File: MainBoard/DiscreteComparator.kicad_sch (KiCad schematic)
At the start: 22 parts, among them Q17 BC557, Q18 BC557, Q19 BC557, Q20 BC557, Q21 BC557, Q22 BC557, Q23 BC557, Q24 BC557, Q25 BC557, Q26 BC547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

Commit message: dealt j8 pin 2 issue by just leaving pine 2 NC
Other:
- note added: "open-collector"
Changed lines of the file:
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@@
+		)
+	)
+	(text "open-collector"
+		(exclude_from_sim no)
+		(at 217.932 86.868 0)
+		(effects
+			(font
+				(size 1.27 1.27)
+			)
 		)
 	)

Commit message: Added bakers clamp on the inverting output transitors to deal with the transtion voltage spikes
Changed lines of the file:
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@@
 		(dnp no)
 		(property "Reference" "Q28"
-			(at 190.754 94.234 0)
+			(at 193.294 104.648 0)
 			(effects
 				(font
@@
 		)
 		(property "Value" "BC547"
-			(at 190.754 96.774 0)
+			(at 191.008 106.934 0)
 			(effects
 				(font
@@
 		(on_board yes)
 		(dnp no)
-		(fields_autoplaced yes)
 		(property "Reference" "Q29"
-			(at 190.5 104.1399 0)
+			(at 178.816 107.696 0)
 			(effects
 				(font
@@
 		)
 		(property "Value" "BC547"
-			(at 190.5 106.6799 0)
-			(effects
-				(font
+			(at 178.816 110.236 0)
+			(effects
+				(font

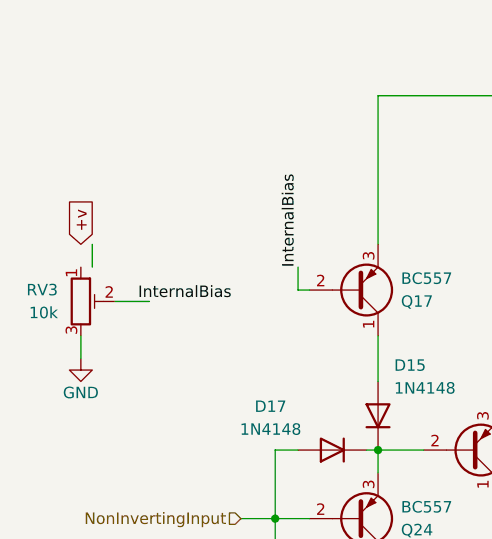
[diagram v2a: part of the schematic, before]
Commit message: added decouping caps to input jack
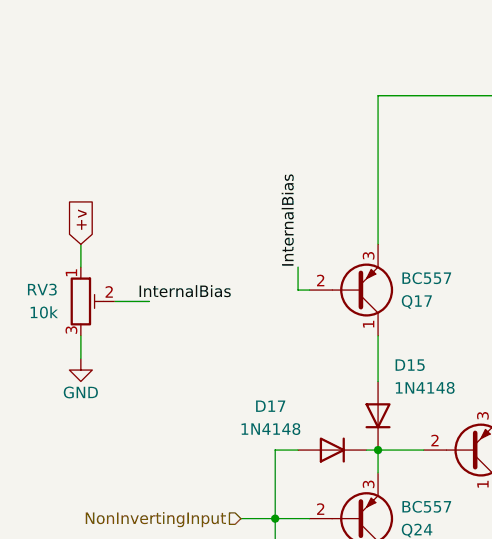
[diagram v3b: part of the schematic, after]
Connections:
- net +v: now also RV3.1
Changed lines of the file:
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@@
 	(wire
 		(pts
-			(xy 68.58 59.69) (xy 68.58 62.23)
+			(xy 67.31 59.69) (xy 67.31 62.23)
 		)
 		(stroke

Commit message: some general clean up
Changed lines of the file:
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@@
 	(wire
 		(pts
-			(xy 71.12 66.04) (xy 74.93 66.04)
+			(xy 71.12 66.04) (xy 73.66 66.04)
 		)
 		(stroke

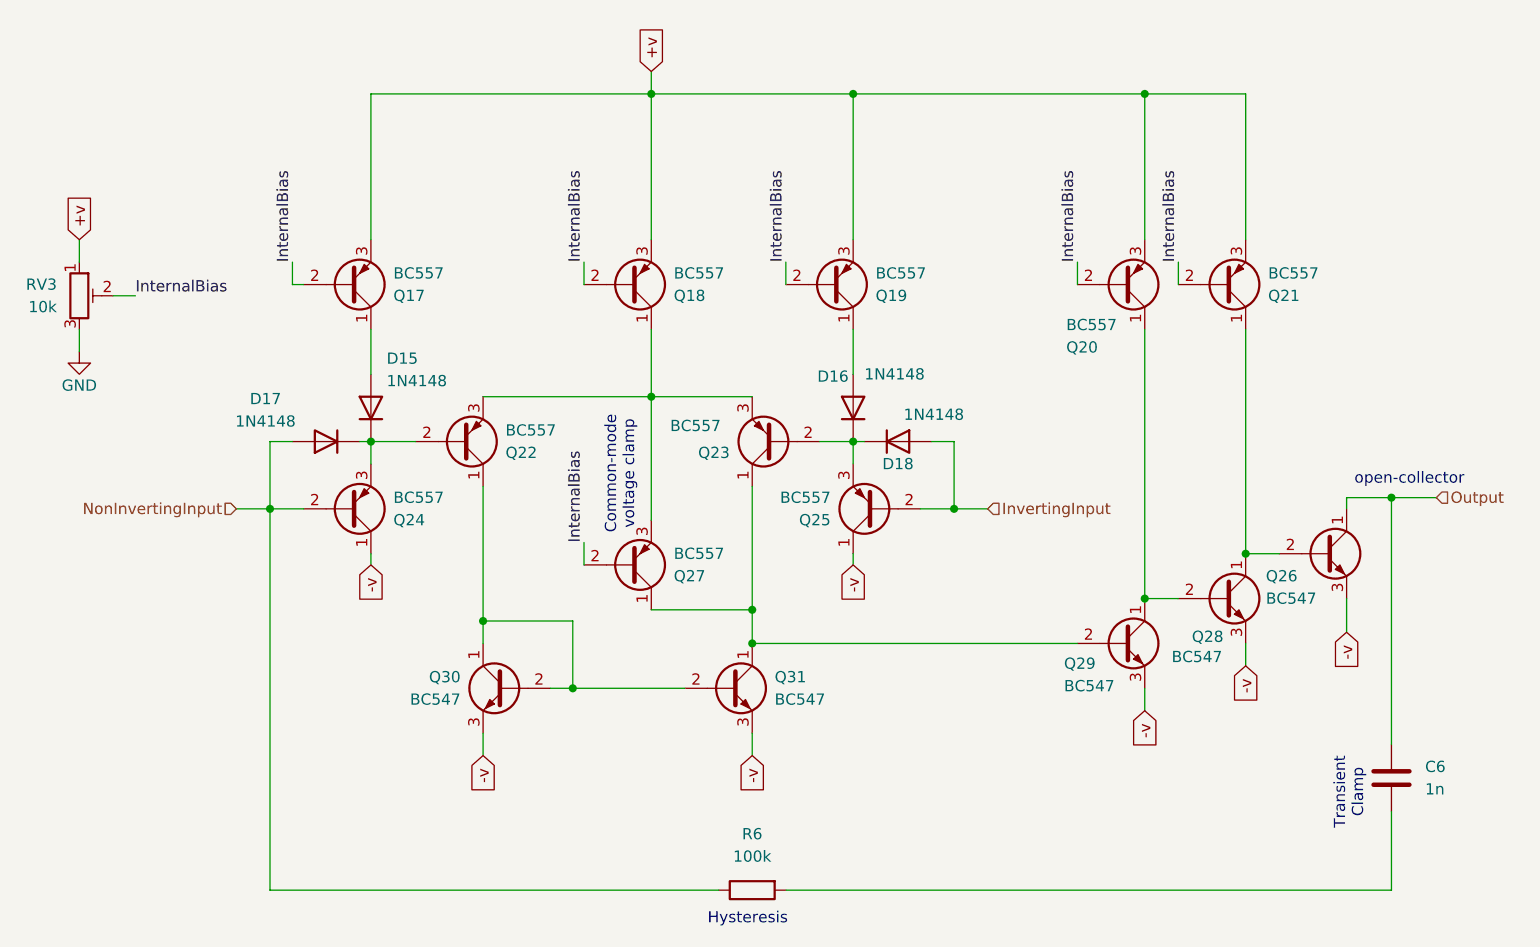
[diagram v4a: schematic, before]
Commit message: refactored power supply
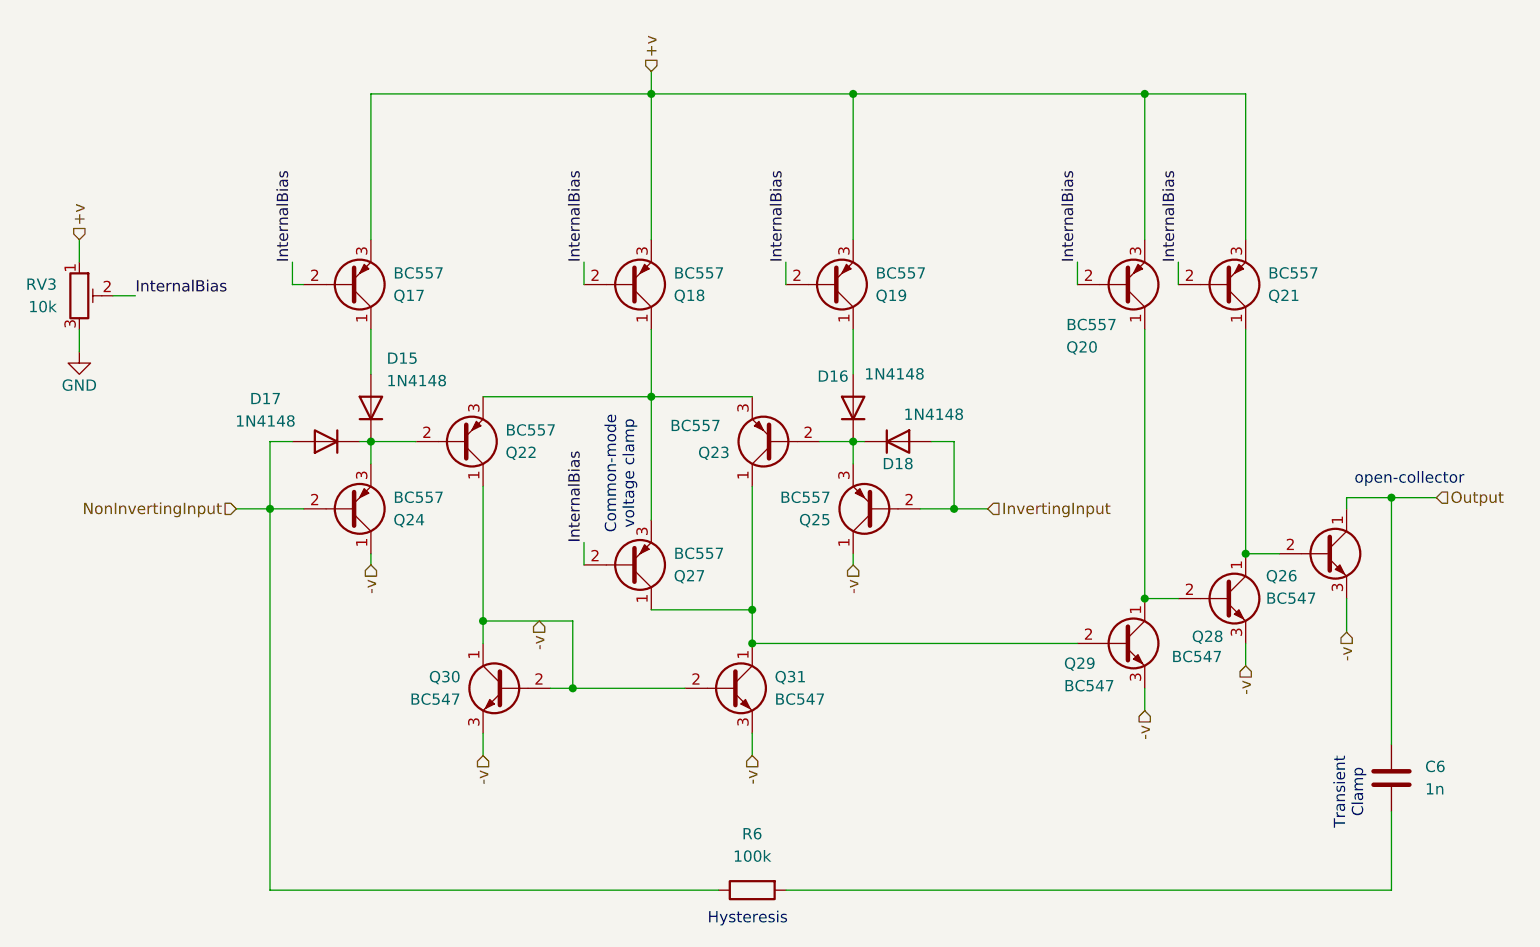
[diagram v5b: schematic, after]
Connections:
- net -v: now also Q22.1 (C), Q30.1 (C), Q30.2 (B), Q31.2 (B)
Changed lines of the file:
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@@
 		)
 	)
-	(global_label "-v"
+	(hierarchical_label "-v"
 		(shape input)
-		(at 199.39 107.95 270)
-		(fields_autoplaced yes)
+		(at 143.51 118.11 270)
 		(effects
 			(font
@@
 			(justify right)
 		)
-		(property "Intersheetrefs" "${INTERSHEET_REFS}"
-			(at 199.39 113.4752 90)
-			(effects
-				(font
-					(size 1.27 1.27)
-				)
-				(justify right)
-				(hide yes)
-			)
-		)
 	)
-	(global_label "-v"
+	(hierarchical_label "-v"
 		(shape input)
-		(at 154.94 96.52 270)
-		(fields_autoplaced yes)
+		(at 119.38 102.87 270)
 		(effects
 			(font
@@
 			(justify right)
 		)
-		(property "Intersheetrefs" "${INTERSHEET_REFS}"
-			(at 154.94 102.0452 90)
-			(effects
-				(font
-					(size 1.27 1.27)
-				)
-				(justify right)
-				(hide yes)
-			)
-		)
 	)
-	(global_label "-v"
+	(hierarchical_label "-v"
 		(shape input)
-		(at 100.33 96.52 270)
-		(fields_autoplaced yes)
+		(at 113.03 118.11 270)
 		(effects
 			(font
@@
 			(justify right)
 		)
-		(property "Intersheetrefs" "${INTERSHEET_REFS}"
-			(at 100.33 102.0452 90)
-			(effects
-				(font
-					(size 1.27 1.27)
-				)
-				(justify right)
-				(hide yes)
-			)
-		)
 	)
-	(global_label "-v"
+	(hierarchical_label "-v"
 		(shape input)
-		(at 187.96 113.03 270)
-		(fields_autoplaced yes)
+		(at 199.39 107.95 270)
 		(effects
 			(font
@@
 			(justify right)
 		)
-		(property "Intersheetrefs" "${INTERSHEET_REFS}"
-			(at 187.96 118.5552 90)
-			(effects
-				(font
-					(size 1.27 1.27)
-				)
-				(justify right)
-				(hide yes)
-			)
-		)
 	)
-	(global_label "-v"
-		(shape input)
-		(at 210.82 104.14 270)
-		(fields_autoplaced yes)
-		(effects
-			(font
-				(size 1.27 1.27)
-			)
-			(justify right)
-		)
-		(property "Intersheetrefs" "${INTERSHEET_REFS}"
-			(at 210.82 109.6652 90)
-			(effects
-				(font
-					(size 1.27 1.27)
-				)
-				(justify right)
-				(hide yes)
-			)
-		)
-	)
-	(global_label "+v"
+	(hierarchical_label "+v"
 		(shape input)
 		(at 67.31 59.69 90)
-		(fields_autoplaced yes)
 		(effects
 			(font
@@
 			(justify left)
 		)
-		(property "Intersheetrefs" "${INTERSHEET_REFS}"
-			(at 67.31 54.1648 90)
-			(effects
-				(font
-					(size 1.27 1.27)
-				)
-				(justify left)
-				(hide yes)
-			)
-		)
 	)
-	(global_label "-v"
+	(hierarchical_label "-v"
 		(shape input)
-		(at 143.51 118.11 270)
-		(fields_autoplaced yes)
+		(at 154.94 96.52 270)
 		(effects
 			(font
@@
 			)
 			(justify right)
-		)
-		(property "Intersheetrefs" "${INTERSHEET_REFS}"
-			(at 143.51 123.6352 90)
-			(effects
-				(font
-					(size 1.27 1.27)
-				)
-				(justify right)
-				(hide yes)
-			)
-		)
-	)
-	(global_label "-v"
-		(shape input)
-		(at 113.03 118.11 270)
-		(fields_autoplaced yes)
-		(effects
-			(font
-				(size 1.27 1.27)
-			)
-			(justify right)
-		)
-		(property "Intersheetrefs" "${INTERSHEET_REFS}"
-			(at 113.03 123.6352 90)
-			(effects
-				(font
-					(size 1.27 1.27)
-				)
-				(justify right)
-				(hide yes)
-			)
-		)
-	)
-	(global_label "+v"
-		(shape input)
-		(at 132.08 40.64 90)
-		(fields_autoplaced yes)
-		(effects
-			(font
-				(size 1.27 1.27)
-			)
-			(justify left)
-		)
-		(property "Intersheetrefs" "${INTERSHEET_REFS}"
-			(at 132.08 35.1148 90)
-			(effects
-				(font
-					(size 1.27 1.27)
-				)
-				(justify left)
-				(hide yes)
-			)
 		)
 	)
@@
 			)
 			(justify left)
+		)
+	)
+	(hierarchical_label "+v"
+		(shape input)
+		(at 132.08 40.64 90)
+		(effects
+			(font
+				(size 1.27 1.27)
+			)
+			(justify left)
+		)
+	)
+	(hierarchical_label "-v"
+		(shape input)
+		(at 100.33 96.52 270)
+		(effects
+			(font
+				(size 1.27 1.27)
+			)
+			(justify right)
+		)
+	)
+	(hierarchical_label "-v"
+		(shape input)
+		(at 210.82 104.14 270)
+		(effects
+			(font
+				(size 1.27 1.27)
+			)
+			(justify right)
 		)
 	)
@@
 		)
 	)
+	(hierarchical_label "-v"
+		(shape input)
+		(at 187.96 113.03 270)
+		(effects
+			(font
+				(size 1.27 1.27)
+			)
+			(justify right)
+		)
+	)
